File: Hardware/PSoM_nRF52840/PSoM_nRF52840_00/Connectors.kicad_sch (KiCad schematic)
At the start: 7 parts, among them J101 DF40C-60DP-0.4V(51), J102 Bare PCB USB C

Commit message: working on nrf52840
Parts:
- removed R101, R102: 5.1k, Resistor_SMD:R_0201_0603Metric, symbol Component lib:R
- renumbered R103 to R101, R104 to R102
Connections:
- net EN renamed RST
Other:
- note added: "100-Connectors"
- note removed: "100-USB"

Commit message: working on schematic
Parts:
- removed C101: 100n, Capacitor_SMD:C_0201_0603Metric, symbol Component lib:C
- removed R101: 220k, Resistor_SMD:R_0201_0603Metric, symbol Component_lib:R
- removed R102: 470k, Resistor_SMD:R_0201_0603Metric, symbol Component_lib:R
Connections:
- net IO10 renamed P21
- net IO11 renamed P23
- net IO12 renamed P25
- net IO13 renamed P27
- net IO14 renamed P29
- net IO15 renamed P31
- net IO16 renamed P33
- net IO17 renamed P35
- net IO18 renamed P37
- net IO2 renamed P5
- net IO21 renamed P39
- net IO3 renamed P7
- net IO33 renamed P30
- net IO34 renamed P32
- net IO35 renamed P34
- net IO36 renamed P36
- net IO37 renamed P38
- net IO38 renamed P40
- net IO39 renamed P44
- net IO4 renamed P9
- net IO40 renamed P46
- net IO41 renamed P42
- net IO42: no longer names the net of J101.52
- net IO5 renamed P11
- net IO6 renamed P13
- net IO7 renamed P15
- net IO8 renamed P17
- net IO9 renamed P19
- net RX0 renamed P52
- net TX0: no longer names the net of J101.50
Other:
- note removed: "6uA leakage"

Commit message: moved in the nrf inside of boundries
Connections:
- net P52: now also J101.52; no longer J101.48
- net SWDCLK: now also J101.48
- net SWDIO: now also J101.50

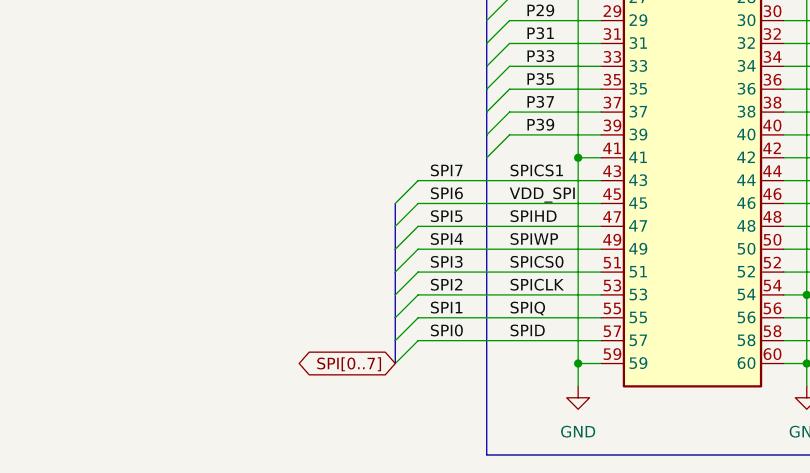
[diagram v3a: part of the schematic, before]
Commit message: moved a few traces
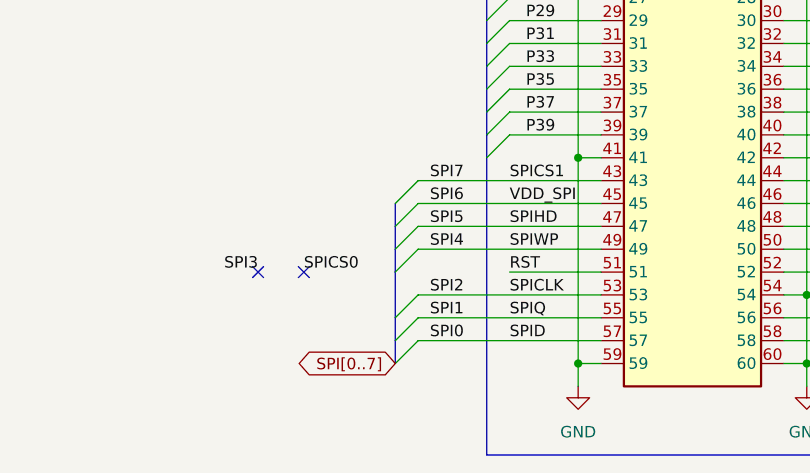
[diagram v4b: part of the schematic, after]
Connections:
- net RST: now also J101.51
- net SPI3: no longer J101.51
- no-connect marks 2 -> 4
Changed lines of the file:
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@@
+	)
+	(no_connect
+		(at 111.76 119.38)
 	)
 	(no_connect
 		(at 63.5 78.74)
 	)
+	(no_connect
+		(at 116.84 119.38)
+	)
 	(bus_entry
 		(at 137.16 71.12)
@@
 	)
 	(bus_entry
-		(at 129.54 116.84)
-		(size -2.54 2.54)
-		(stroke
-			(width 0)
-			(type default)
-		)
-	)
-	(bus_entry
 		(at 139.7 99.06)
 		(size -2.54 2.54)
@@
 	)
 	(bus_entry
+		(at 127 119.38)
+		(size 2.54 -2.54)
+		(stroke
+			(width 0)
+			(type default)
+		)
+	)
+	(bus_entry
 		(at 139.7 81.28)
 		(size -2.54 2.54)
@@
 	)
 	(bus_entry
-		(at 129.54 119.38)
-		(size -2.54 2.54)
-		(stroke
-			(width 0)
-			(type default)
-		)
-	)
-	(bus_entry
 		(at 129.54 111.76)
 		(size -2.54 2.54)
@@
 		)
 	)
-	(wire
-		(pts
-			(xy 129.54 119.38) (xy 149.86 119.38)
-		)
-		(stroke
-			(width 0)
-			(type default)
-		)
-	)
 	(bus
 		(pts
@@
 		)
 	)
+	(bus
+		(pts
+			(xy 127 119.38) (xy 127 124.46)
+		)
+		(stroke
+			(width 0)
+			(type default)
+		)
+	)
 	(wire
 		(pts
@@
 		)
 	)
+	(wire
+		(pts
+			(xy 139.7 119.38) (xy 149.86 119.38)
+		)
+		(stroke
+			(width 0)
+			(type default)
+		)
+	)
 	(bus
 		(pts
@@
 	(bus
 		(pts
-			(xy 127 119.38) (xy 127 116.84)
+			(xy 127 116.84) (xy 127 119.38)
 		)
 		(stroke
@@
 		)
 	)
-	(bus
-		(pts
-			(xy 127 124.46) (xy 127 121.92)
-		)
-		(stroke
-			(width 0)
-			(type default)
-		)
-	)
 	(wire
 		(pts
@@
 		(pts
 			(xy 127 129.54) (xy 127 127)
-		)
-		(stroke
-			(width 0)
-			(type default)
-		)
-	)
-	(bus
-		(pts
-			(xy 127 121.92) (xy 127 119.38)
 		)
 		(stroke
@@
 		)
 	)
+	(label "SPICS0"
+		(at 116.84 119.38 0)
+		(effects
+			(font
+				(size 1.27 1.27)
+			)
+			(justify left bottom)
+		)
+	)
 	(label "BATTERY_TEMP"
 		(at 256.54 50.8 180)
@@
 		)
 	)
+	(label "SPI3"
+		(at 111.76 119.38 180)
+		(effects
+			(font
+				(size 1.27 1.27)
+			)
+			(justify right bottom)
+		)
+	)
 	(label "SPICS1"
 		(at 139.7 109.22 0)
@@
 		)
 	)
+	(label "RST"
+		(at 139.7 119.38 0)
+		(effects
+			(font
+				(size 1.27 1.27)
+			)
+			(justify left bottom)
+		)
+	)
 	(label "VDD_SPI"
 		(at 139.7 111.76 0)
@@
 		)
 	)
-	(label "SPI3"
-		(at 134.62 119.38 180)
-		(effects
-			(font
-				(size 1.27 1.27)
-			)
-			(justify right bottom)
-		)
-	)
 	(label "CC1"
 		(at 66.04 55.88 0)
@@
 		)
 	)
-	(label "SPICS0"
-		(at 139.7 119.38 0)
-		(effects
-			(font
-				(size 1.27 1.27)
-			)
-			(justify left bottom)
-		)
-	)

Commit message: schematic should be done
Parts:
- removed J102: Bare PCB USB C, Component_lib:usb-c-pcb, symbol Component_lib:Bare PCB USB C
- added J1: Bare PCB USB C, Component_lib:usb-c-pcb, symbol Component_lib:Bare PCB USB C_3.0
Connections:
- net CC1: now also J1.A5 (CC1)
- net CC2: now also J1.B5 (CC2)
- net D+: now also J1.A6 (D+), J1.B6 (D+)
- net D-: now also J1.A7 (D-), J1.B7 (D-)
- net GND: now also J101.61 (Mount), J101.62, J101.63, J101.64, J1.A1 (GND_1), J1.A12 (GND_2), J1.B1 (GND_3), J1.B12 (GND_4)
- net VBUS: now also J1.A4 (VBUS), J1.A9 (VBUS), J1.B4 (VBUS), J1.B9 (VBUS)
- net IO0: no longer names the net of J101.26
- no-connect marks 4 -> 13
